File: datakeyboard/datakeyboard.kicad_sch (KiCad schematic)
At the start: 45 parts, among them Q1 BSS83P, Q2 BSS83P, Q3 BSS83P, Q4 BSS83P, SW1 SW_Push, SW2 SW_Push, SW3 SW_Push, SW4 SW_Push, SW5 SW_Push, SW6 SW_Push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

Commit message: Resize solder pads
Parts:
- removed JBAT1, JCASE1: Conn_01x02, Resistor_SMD:R_1206_3216Metric_Pad1.30x1.75mm_HandSolder, symbol Connector_Generic:Conn_01x02
- added JBAT1, JBAT2, JCASE1, JCASE2: Conn_01x01, TestPoint:TestPoint_Pad_2.0x2.0mm, symbol Connector_Generic:Conn_01x01
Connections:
- net CASE: now also JCASE1.1 (Pin_1)
- net GND: now also JBAT2.1 (Pin_1), JCASE2.1 (Pin_1)
- net VBAT: now also JBAT1.1 (Pin_1)
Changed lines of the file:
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@@
+    (stroke (width 0) (type default) (color 0 0 0 0))
+  )
+  (wire (pts (xy 95.25 33.02) (xy 95.25 34.29))
     (stroke (width 0) (type default) (color 0 0 0 0))
   )
@@
     (stroke (width 0) (type default) (color 0 0 0 0))
   )
-  (wire (pts (xy 88.9 26.67) (xy 88.9 38.1))
+  (wire (pts (xy 88.9 33.02) (xy 88.9 38.1))
     (stroke (width 0) (type default) (color 0 0 0 0))
   )
@@
     (stroke (width 0) (type default) (color 0 0 0 0))
   )
-  (wire (pts (xy 144.78 26.67) (xy 144.78 67.31))
+  (wire (pts (xy 144.78 33.02) (xy 144.78 67.31))
     (stroke (width 0) (type default) (color 0 0 0 0))
   )
@@
     (stroke (width 0) (type default) (color 0 0 0 0))
   )
-  (wire (pts (xy 147.32 26.67) (xy 147.32 27.94))
-    (stroke (width 0) (type default) (color 0 0 0 0))
-  )
   (wire (pts (xy 97.79 66.04) (xy 99.06 66.04))
     (stroke (width 0) (type default) (color 0 0 0 0))
@@
     (stroke (width 0) (type default) (color 0 0 0 0))
   )
-  (wire (pts (xy 91.44 26.67) (xy 91.44 29.21))
-    (stroke (width 0) (type default) (color 0 0 0 0))
-  )
   (wire (pts (xy 149.86 64.77) (xy 149.86 67.31))
     (stroke (width 0) (type default) (color 0 0 0 0))
@@
   )
   (wire (pts (xy 50.8 179.07) (xy 62.23 179.07))
+    (stroke (width 0) (type default) (color 0 0 0 0))
+  )
+  (wire (pts (xy 151.13 33.02) (xy 151.13 34.29))
     (stroke (width 0) (type default) (color 0 0 0 0))
   )
@@
     (pin "2")
   )
+  (symbol (lib_id "Connector_Generic:Conn_01x01") (at 151.13 27.94 90) (unit 1)
+    (in_bom yes) (on_board yes)
+    (property "Reference" "JCASE2" (id 0) (at 148.59 20.32 0)
+      (effects (font (size 1.27 1.27)) (justify right))
+    )
+    (property "Value" "Conn_01x01" (id 1) (at 151.13 13.97 0)
+      (effects (font (size 1.27 1.27)) (justify right))
+    )
+    (property "Footprint" "TestPoint:TestPoint_Pad_2.0x2.0mm" (id 2) (at 151.13 27.94 0)
+      (effects (font (size 1.27 1.27)) hide)
+    )
+    (property "Datasheet" "~" (id 3) (at 151.13 27.94 0)
+      (effects (font (size 1.27 1.27)) hide)
+    )
+    (pin "1")
+  )
   (symbol (lib_id "Device:C_Small") (at 62.23 176.53 0) (unit 1)
     (in_bom yes) (on_board yes) (fields_autoplaced)
@@
     (pin "1")
     (pin "2")
+  )
+  (symbol (lib_id "Connector_Generic:Conn_01x01") (at 144.78 27.94 90) (unit 1)
+    (in_bom yes) (on_board yes)
+    (property "Reference" "JCASE1" (id 0) (at 142.24 20.32 0)
+      (effects (font (size 1.27 1.27)) (justify right))
+    )
+    (property "Value" "Conn_01x01" (id 1) (at 144.78 13.97 0)
+      (effects (font (size 1.27 1.27)) (justify right))
+    )
+    (property "Footprint" "TestPoint:TestPoint_Pad_2.0x2.0mm" (id 2) (at 144.78 27.94 0)
+      (effects (font (size 1.27 1.27)) hide)
+    )
+    (property "Datasheet" "~" (id 3) (at 144.78 27.94 0)
+      (effects (font (size 1.27 1.27)) hide)
+    )
+    (pin "1")
   )
   (symbol (lib_id "Device:LED") (at 76.2 29.21 90) (unit 1)
@@
     (pin "1")
   )
-  (symbol (lib_id "power:GND") (at 147.32 27.94 0) (unit 1)
-    (in_bom yes) (on_board yes) (fields_autoplaced)
-    (property "Reference" "#PWR0108" (id 0) (at 147.32 34.29 0)
-      (effects (font (size 1.27 1.27)) hide)
-    )
-    (property "Value" "GND" (id 1) (at 147.32 33.02 0))
-    (property "Footprint" "" (id 2) (at 147.32 27.94 0)
-      (effects (font (size 1.27 1.27)) hide)
-    )
-    (property "Datasheet" "" (id 3) (at 147.32 27.94 0)
+  (symbol (lib_id "power:GND") (at 151.13 34.29 0) (unit 1)
+    (in_bom yes) (on_board yes) (fields_autoplaced)
+    (property "Reference" "#PWR0108" (id 0) (at 151.13 40.64 0)
+      (effects (font (size 1.27 1.27)) hide)
+    )
+    (property "Value" "GND" (id 1) (at 151.13 39.37 0))
+    (property "Footprint" "" (id 2) (at 151.13 34.29 0)
+      (effects (font (size 1.27 1.27)) hide)
+    )
+    (property "Datasheet" "" (id 3) (at 151.13 34.29 0)
       (effects (font (size 1.27 1.27)) hide)
     )
@@
     (pin "2")
   )
-  (symbol (lib_id "Connector_Generic:Conn_01x02") (at 144.78 21.59 90) (unit 1)
-    (in_bom yes) (on_board yes) (fields_autoplaced)
-    (property "Reference" "JCASE1" (id 0) (at 149.86 20.3199 90)
+  (symbol (lib_id "Connector_Generic:Conn_01x01") (at 95.25 27.94 90) (unit 1)
+    (in_bom yes) (on_board yes)
+    (property "Reference" "JBAT2" (id 0) (at 92.71 20.32 0)
       (effects (font (size 1.27 1.27)) (justify right))
     )
-    (property "Value" "Conn_01x02" (id 1) (at 149.86 22.8599 90)
+    (property "Value" "Conn_01x01" (id 1) (at 95.25 13.97 0)
       (effects (font (size 1.27 1.27)) (justify right))
     )
-    (property "Footprint" "Resistor_SMD:R_1206_3216Metric_Pad1.30x1.75mm_HandSolder" (id 2) (at 144.78 21.59 0)
-      (effects (font (size 1.27 1.27)) hide)
-    )
-    (property "Datasheet" "~" (id 3) (at 144.78 21.59 0)
-      (effects (font (size 1.27 1.27)) hide)
-    )
-    (pin "1")
-    (pin "2")
+    (property "Footprint" "TestPoint:TestPoint_Pad_2.0x2.0mm" (id 2) (at 95.25 27.94 0)
+      (effects (font (size 1.27 1.27)) hide)
+    )
+    (property "Datasheet" "~" (id 3) (at 95.25 27.94 0)
+      (effects (font (size 1.27 1.27)) hide)
+    )
+    (pin "1")
   )
   (symbol (lib_id "power:GND") (at 217.17 58.42 270) (unit 1)
@@
     (pin "3")
   )
-  (symbol (lib_id "Connector_Generic:Conn_01x02") (at 88.9 21.59 90) (unit 1)
-    (in_bom yes) (on_board yes) (fields_autoplaced)
-    (property "Reference" "JBAT1" (id 0) (at 93.98 20.3199 90)
+  (symbol (lib_id "Connector_Generic:Conn_01x01") (at 88.9 27.94 90) (unit 1)
+    (in_bom yes) (on_board yes)
+    (property "Reference" "JBAT1" (id 0) (at 86.36 20.32 0)
       (effects (font (size 1.27 1.27)) (justify right))
     )
-    (property "Value" "Conn_01x02" (id 1) (at 93.98 22.8599 90)
+    (property "Value" "Conn_01x01" (id 1) (at 88.9 13.97 0)
       (effects (font (size 1.27 1.27)) (justify right))
     )
-    (property "Footprint" "Resistor_SMD:R_1206_3216Metric_Pad1.30x1.75mm_HandSolder" (id 2) (at 88.9 21.59 0)
-      (effects (font (size 1.27 1.27)) hide)
-    )
-    (property "Datasheet" "~" (id 3) (at 88.9 21.59 0)
-      (effects (font (size 1.27 1.27)) hide)
-    )
-    (pin "1")
-    (pin "2")
+    (property "Footprint" "TestPoint:TestPoint_Pad_2.0x2.0mm" (id 2) (at 88.9 27.94 0)
+      (effects (font (size 1.27 1.27)) hide)
+    )
+    (property "Datasheet" "~" (id 3) (at 88.9 27.94 0)
+      (effects (font (size 1.27 1.27)) hide)
+    )
+    (pin "1")
   )
   (symbol (lib_id "power:GND") (at 162.56 151.13 0) (unit 1)
@@
     (pin "1")
   )
-  (symbol (lib_id "power:GND") (at 91.44 29.21 0) (unit 1)
-    (in_bom yes) (on_board yes) (fields_autoplaced)
-    (property "Reference" "#PWR07" (id 0) (at 91.44 35.56 0)
-      (effects (font (size 1.27 1.27)) hide)
-    )
-    (property "Value" "GND" (id 1) (at 91.44 34.29 0))
-    (property "Footprint" "" (id 2) (at 91.44 29.21 0)
-      (effects (font (size 1.27 1.27)) hide)
-    )
-    (property "Datasheet" "" (id 3) (at 91.44 29.21 0)
+  (symbol (lib_id "power:GND") (at 95.25 34.29 0) (unit 1)
+    (in_bom yes) (on_board yes)
+    (property "Reference" "#PWR07" (id 0) (at 95.25 40.64 0)
+      (effects (font (size 1.27 1.27)) hide)
+    )
+    (property "Value" "GND" (id 1) (at 92.71 34.29 0))
+    (property "Footprint" "" (id 2) (at 95.25 34.29 0)
+      (effects (font (size 1.27 1.27)) hide)
+    )
+    (property "Datasheet" "" (id 3) (at 95.25 34.29 0)
       (effects (font (size 1.27 1.27)) hide)
     )
@@
       (reference "D2") (unit 1) (value "LED") (footprint "LED_SMD:LED_0805_2012Metric_Pad1.15x1.40mm_HandSolder")
     )
-    (path "/a3fb3ec1-d439-4e28-9c23-0b3ef6bab1e5"
-      (reference "JBAT1") (unit 1) (value "Conn_01x02") (footprint "Resistor_SMD:R_1206_3216Metric_Pad1.30x1.75mm_HandSolder")
+    (path "/a4652af2-11f3-4247-9dfd-87dfbd12435c"
+      (reference "JBAT1") (unit 1) (value "Conn_01x01") (footprint "TestPoint:TestPoint_Pad_2.0x2.0mm")
+    )
+    (path "/9d330284-144a-4057-8bc0-cd243b204a16"
+      (reference "JBAT2") (unit 1) (value "Conn_01x01") (footprint "TestPoint:TestPoint_Pad_2.0x2.0mm")
     )
     (path "/736d6c1c-614a-4b0f-8fe3-6b0669b7a1b9"
       (reference "JCARD1") (unit 1) (value "Micro_SD_Card_Det") (footprint "Library:microSD_Unknown")
     )
-    (path "/a0d77163-a822-4f35-a314-d39c42d23672"
-      (reference "JCASE1") (unit 1) (value "Conn_01x02") (footprint "Resistor_SMD:R_1206_3216Metric_Pad1.30x1.75mm_HandSolder")
+    (path "/61d52993-c058-4971-be2f-89a53f181c99"
+      (reference "JCASE1") (unit 1) (value "Conn_01x01") (footprint "TestPoint:TestPoint_Pad_2.0x2.0mm")
+    )
+    (path "/4e8cbafb-6e04-442d-9ca1-84b3b64a4f52"
+      (reference "JCASE2") (unit 1) (value "Conn_01x01") (footprint "TestPoint:TestPoint_Pad_2.0x2.0mm")
     )
     (path "/d37334a6-f13d-49cb-afe8-430745ecfc0f"

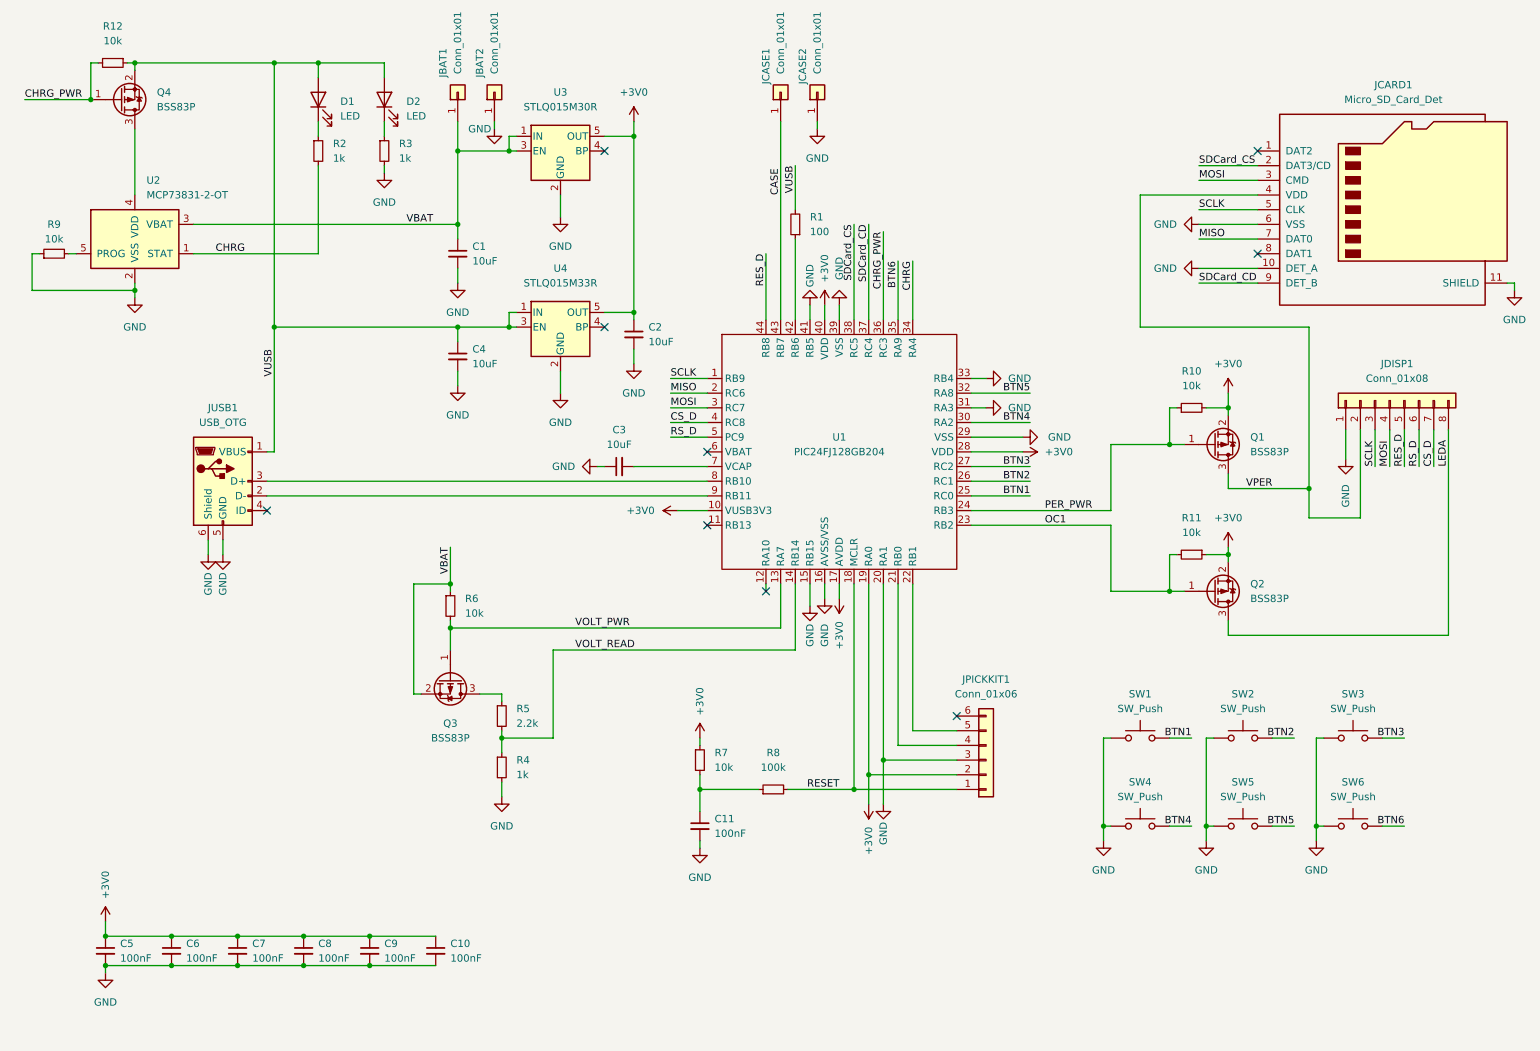
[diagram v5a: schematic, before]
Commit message: Redesign power supply to bypass charger when running from USB
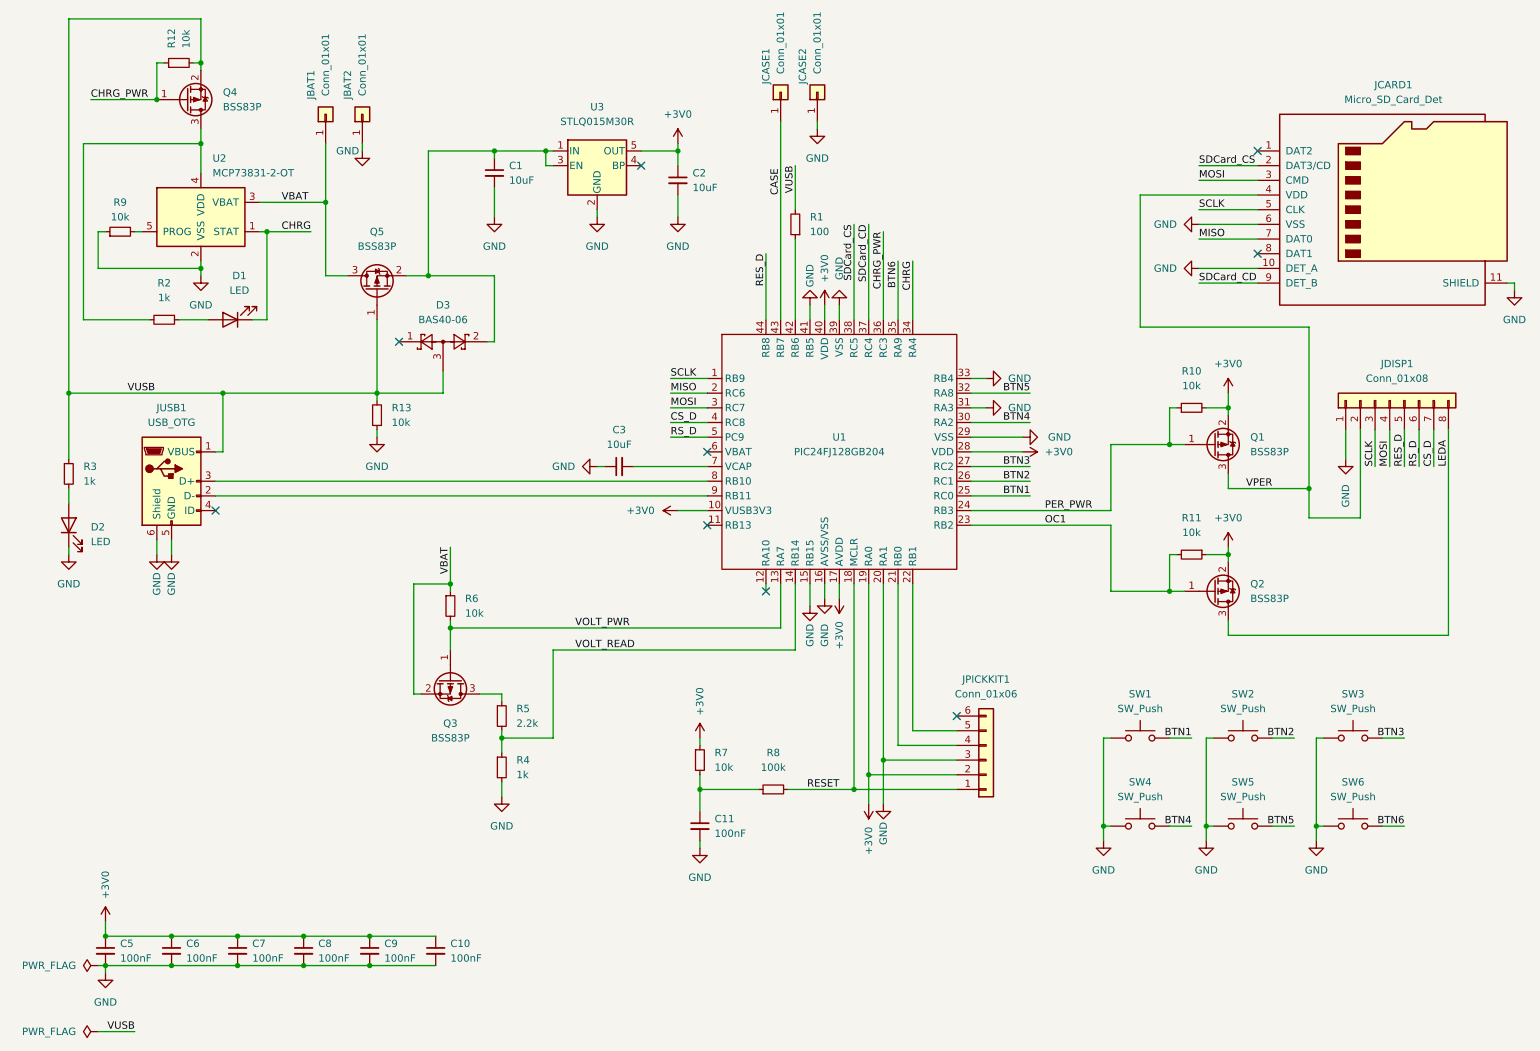
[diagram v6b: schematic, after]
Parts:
- removed C4: 10uF, Capacitor_SMD:C_0805_2012Metric_Pad1.18x1.45mm_HandSolder, symbol Device:C_Small
- removed U4: STLQ015M33R, Package_TO_SOT_SMD:SOT-23-5, symbol Regulator_Linear:AP131-30
- added D3: BAS40-06, Package_TO_SOT_SMD:SOT-23, symbol Library:BAS40-06
- added Q5: BSS83P, Package_TO_SOT_SMD:SOT-23, symbol Transistor_FET:BSS83P
- added R13: 10k, Resistor_SMD:R_0805_2012Metric_Pad1.20x1.40mm_HandSolder, symbol Device:R_Small
- D1, D2: footprint LED_SMD:LED_0805_2012Metric_Pad1.15x1.40mm_HandSolder -> Diode_SMD:D_1206_3216Metric_Pad1.42x1.75mm_HandSolder
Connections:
- net CHRG: now also D1.1 (K); no longer R2.2
- net CHRG_PWR: now also R12.1; no longer R12.2
- net GND: now also D2.1 (K), R13.1; no longer R3.2
- net VBAT: now also Q5.3 (D); no longer C1.1, U3.1 (IN), U3.3 (EN)
- net VUSB: now also R12.2, R3.1, D3.3, Q5.1 (G), R13.2; no longer D1.2 (A), D2.2 (A), R12.1
- net at Q4.3 (D), U2.4 (VDD): now also R2.2
- net at R2.1: now also D1.2 (A); no longer D1.1 (K)
- new net: C1.1, D3.2, Q5.2 (S), U3.1 (IN), U3.3 (EN)
- new net: D2.2 (A), R3.2
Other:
- moved on the sheet: C1, C2, D1, D2, JBAT1, JBAT2, JUSB1, R2, R3, R9, U2, U3
